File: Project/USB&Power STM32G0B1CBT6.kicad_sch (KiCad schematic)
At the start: 16 parts, among them J1 JST SH, J12 USB_C sink board 1.3mm, J2 Pico EZmate, Q1 AP40P05, U58 PRTR5V0U2X, U64 AP2112K-3.3

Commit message: backups
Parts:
- renumbered C53 to C59, C55 to C60, J12 to J2, R8 to R6, U64 to U54
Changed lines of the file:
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@@
 				)
 				(path "/7fa06d8b-464b-4050-a0fd-d319cc509390/482325c2-4a62-42d2-bd7f-adb26184afc4"
-					(reference "C62")
+					(reference "C61")
 					(unit 1)
 				)
@@
 				)
 				(path "/7fa06d8b-464b-4050-a0fd-d319cc509390/482325c2-4a62-42d2-bd7f-adb26184afc4"
-					(reference "#PWR0175")
+					(reference "#PWR0177")
 					(unit 1)
 				)
@@
 		(dnp no)
 		(fields_autoplaced yes)
-		(property "Reference" "U64"
+		(property "Reference" "U54"
 			(at 130.81 25.4 0)
 			(effects
@@
 			(project "vootington V4N STM32G0B1CBT6"
 				(path "/7fa06d8b-464b-4050-a0fd-d319cc509390/482325c2-4a62-42d2-bd7f-adb26184afc4"
-					(reference "U64")
+					(reference "U54")
 					(unit 1)
 				)
@@
 		(on_board yes)
 		(dnp no)
-		(property "Reference" "#PWR0169"
+		(property "Reference" "#PWR0174"
 			(at 153.035 71.12 0)
 			(effects
@@
 			(project "vootington V4N STM32G0B1CBT6"
 				(path "/7fa06d8b-464b-4050-a0fd-d319cc509390/482325c2-4a62-42d2-bd7f-adb26184afc4"
-					(reference "#PWR0169")
+					(reference "#PWR0174")
 					(unit 1)
 				)
@@
 		(on_board yes)
 		(dnp no)
-		(property "Reference" "#PWR0157"
+		(property "Reference" "#PWR0170"
 			(at 113.03 53.34 0)
 			(effects
@@
 			(project "vootington V4N STM32G0B1CBT6"
 				(path "/7fa06d8b-464b-4050-a0fd-d319cc509390/482325c2-4a62-42d2-bd7f-adb26184afc4"
-					(reference "#PWR0157")
+					(reference "#PWR0170")
 					(unit 1)
 				)
@@
 			(project "vootington V4N STM32G0B1CBT6"
 				(path "/7fa06d8b-464b-4050-a0fd-d319cc509390/482325c2-4a62-42d2-bd7f-adb26184afc4"
-					(reference "R2")
+					(reference "R7")
 					(unit 1)
 				)
@@
 		(on_board yes)
 		(dnp no)
-		(property "Reference" "R8"
+		(property "Reference" "R6"
 			(at 118.11 43.18 90)
 			(effects
@@
 			(project "vootington V4N STM32G0B1CBT6"
 				(path "/7fa06d8b-464b-4050-a0fd-d319cc509390/482325c2-4a62-42d2-bd7f-adb26184afc4"
-					(reference "R8")
+					(reference "R6")
 					(unit 1)
 				)
@@
 		(dnp no)
 		(fields_autoplaced yes)
-		(property "Reference" "#PWR0174"
+		(property "Reference" "#PWR0176"
 			(at 25.273 86.995 0)
 			(effects
@@
 			(project "vootington V4N STM32G0B1CBT6"
 				(path "/7fa06d8b-464b-4050-a0fd-d319cc509390/482325c2-4a62-42d2-bd7f-adb26184afc4"
-					(reference "#PWR0174")
+					(reference "#PWR0176")
 					(unit 1)
 				)
@@
 		(on_board yes)
 		(dnp no)
-		(property "Reference" "C55"
+		(property "Reference" "C60"
 			(at 101.854 42.672 0)
 			(effects
@@
 			(project "vootington V4N STM32G0B1CBT6"
 				(path "/7fa06d8b-464b-4050-a0fd-d319cc509390/482325c2-4a62-42d2-bd7f-adb26184afc4"
-					(reference "C55")
+					(reference "C60")
 					(unit 1)
 				)
@@
 			(project "vootington V4N STM32G0B1CBT6"
 				(path "/7fa06d8b-464b-4050-a0fd-d319cc509390/482325c2-4a62-42d2-bd7f-adb26184afc4"
-					(reference "J13")
+					(reference "J3")
 					(unit 1)
 				)
@@
 			(project "vootington V4N STM32G0B1CBT6"
 				(path "/7fa06d8b-464b-4050-a0fd-d319cc509390/482325c2-4a62-42d2-bd7f-adb26184afc4"
-					(reference "#PWR0178")
+					(reference "#PWR0180")
 					(unit 1)
 				)
@@
 			(project "vootington V4N STM32G0B1CBT6"
 				(path "/7fa06d8b-464b-4050-a0fd-d319cc509390/482325c2-4a62-42d2-bd7f-adb26184afc4"
-					(reference "#PWR0177")
+					(reference "#PWR0179")
 					(unit 1)
 				)
@@
 		(dnp no)
 		(fields_autoplaced yes)
-		(property "Reference" "#PWR0168"
+		(property "Reference" "#PWR0173"
 			(at 140.335 68.58 0)
 			(effects
@@
 			(project "vootington V4N STM32G0B1CBT6"
 				(path "/7fa06d8b-464b-4050-a0fd-d319cc509390/482325c2-4a62-42d2-bd7f-adb26184afc4"
-					(reference "#PWR0168")
+					(reference "#PWR0173")
 					(unit 1)
 				)
@@
 			(project "vootington V4N STM32G0B1CBT6"
 				(path "/7fa06d8b-464b-4050-a0fd-d319cc509390/482325c2-4a62-42d2-bd7f-adb26184afc4"
-					(reference "#PWR0180")
+					(reference "#PWR0182")
 					(unit 1)
 				)
@@
 			(project "vootington V4N STM32G0B1CBT6"
 				(path "/7fa06d8b-464b-4050-a0fd-d319cc509390/482325c2-4a62-42d2-bd7f-adb26184afc4"
-					(reference "#PWR0176")
+					(reference "#PWR0178")
 					(unit 1)
 				)
@@
 				)
 				(path "/7fa06d8b-464b-4050-a0fd-d319cc509390/482325c2-4a62-42d2-bd7f-adb26184afc4"
-					(reference "#PWR0170")
+					(reference "#PWR0169")
 					(unit 1)
 				)
@@
 				)
 				(path "/7fa06d8b-464b-4050-a0fd-d319cc509390/482325c2-4a62-42d2-bd7f-adb26184afc4"
-					(reference "#PWR0173")
+					(reference "#PWR0175")
 					(unit 1)
 				)
@@
 			(project "vootington V4N STM32G0B1CBT6"
 				(path "/7fa06d8b-464b-4050-a0fd-d319cc509390/482325c2-4a62-42d2-bd7f-adb26184afc4"
-					(reference "#PWR0179")
+					(reference "#PWR0181")
 					(unit 1)
 				)
@@
 				)
 				(path "/7fa06d8b-464b-4050-a0fd-d319cc509390/482325c2-4a62-42d2-bd7f-adb26184afc4"
-					(reference "C60")
+					(reference "C57")
 					(unit 1)
 				)
@@
 			(project "vootington V4N STM32G0B1CBT6"
 				(path "/7fa06d8b-464b-4050-a0fd-d319cc509390/482325c2-4a62-42d2-bd7f-adb26184afc4"
-					(reference "J14")
+					(reference "J4")
 					(unit 1)
 				)
@@
 			(project "vootington V4N STM32G0B1CBT6"
 				(path "/7fa06d8b-464b-4050-a0fd-d319cc509390/482325c2-4a62-42d2-bd7f-adb26184afc4"
-					(reference "#PWR0181")
+					(reference "#PWR0183")
 					(unit 1)
 				)
@@
 		(on_board yes)
 		(dnp no)
-		(property "Reference" "C53"
+		(property "Reference" "C59"
 			(at 148.336 35.306 0)
 			(effects
@@
 			(project "vootington V4N STM32G0B1CBT6"
 				(path "/7fa06d8b-464b-4050-a0fd-d319cc509390/482325c2-4a62-42d2-bd7f-adb26184afc4"
-					(reference "C53")
+					(reference "C59")
 					(unit 1)
 				)
@@
 		(dnp no)
 		(fields_autoplaced yes)
-		(property "Reference" "#PWR0165"
+		(property "Reference" "#PWR0168"
 			(at 140.97 34.29 0)
 			(effects
@@
 			(project "vootington V4N STM32G0B1CBT6"
 				(path "/7fa06d8b-464b-4050-a0fd-d319cc509390/482325c2-4a62-42d2-bd7f-adb26184afc4"
-					(reference "#PWR0165")
+					(reference "#PWR0168")
 					(unit 1)
 				)
@@
 			(project "vootington V4N STM32G0B1CBT6"
 				(path "/7fa06d8b-464b-4050-a0fd-d319cc509390/482325c2-4a62-42d2-bd7f-adb26184afc4"
-					(reference "R3")
+					(reference "R8")
 					(unit 1)
 				)
@@
 				)
 				(path "/7fa06d8b-464b-4050-a0fd-d319cc509390/482325c2-4a62-42d2-bd7f-adb26184afc4"
-					(reference "C61")
+					(reference "C58")
 					(unit 1)
 				)
@@
 		(dnp no)
 		(fields_autoplaced yes)
-		(property "Reference" "J12"
+		(property "Reference" "J2"
 			(at 29.21 33.02 0)
 			(effects
@@
 			(project "vootington V4N STM32G0B1CBT6"
 				(path "/7fa06d8b-464b-4050-a0fd-d319cc509390/482325c2-4a62-42d2-bd7f-adb26184afc4"
-					(reference "J12")
-					(unit 1)
-				)
+					(reference "J2")
+					(unit 1)
+				)

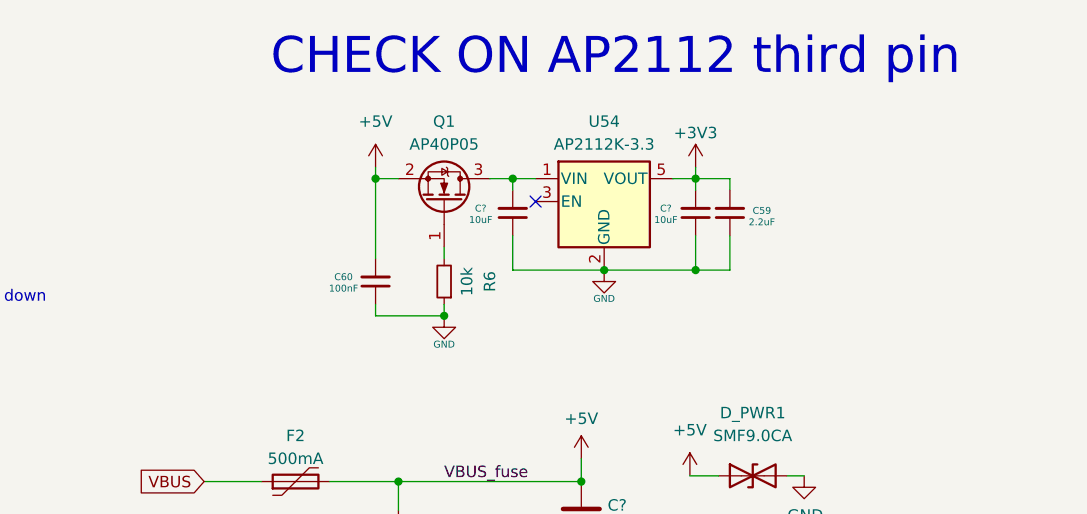
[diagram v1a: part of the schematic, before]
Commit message: power error fix
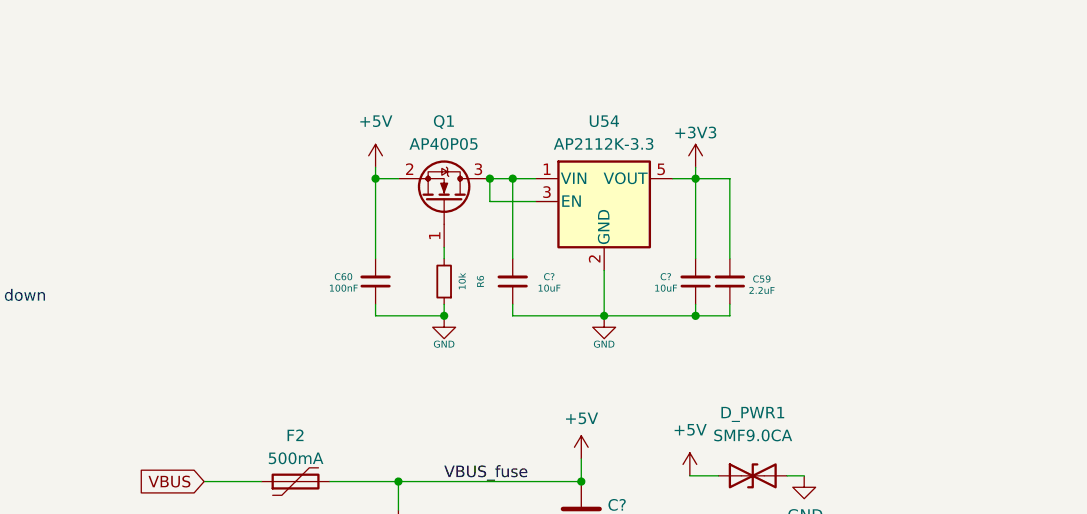
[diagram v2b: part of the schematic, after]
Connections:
- net at C?.2, Q1.3 (D), U54.1 (VIN): now also U54.3 (EN)
- no-connect marks 3 -> 2
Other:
- note removed: "CHECK ON AP2112 third pin"
- moved on the sheet: C59, C?
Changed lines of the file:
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@@
 	)
 	(junction
+		(at 118.11 31.75)
+		(diameter 0)
+		(color 0 0 0 0)
+	)
+	(junction
+		(at 130.81 46.99)
+		(diameter 0)
+		(color 0 0 0 0)
+	)
+	(junction
 		(at 140.97 31.75)
 		(diameter 0)
@@
 	)
 	(junction
-		(at 140.97 41.91)
+		(at 140.97 46.99)
 		(diameter 0)
 		(color 0 0 0 0)
@@
 		(color 0 0 0 0)
 	)
-	(junction
-		(at 130.81 41.91)
-		(diameter 0)
-		(color 0 0 0 0)
-	)
 	(no_connect
 		(at 44.45 68.58)
@@
 		(at 44.45 71.12)
 	)
-	(no_connect
-		(at 123.19 34.29)
-	)
 	(wire
 		(pts
@@
 		)
 	)
-	(bus
-		(pts
-			(xy 13.97 104.775) (xy 49.657 104.775)
-		)
-		(stroke
-			(width 0)
-			(type default)
-		)
-	)
 	(wire
 		(pts
-			(xy 140.97 31.75) (xy 140.97 33.02)
+			(xy 144.78 46.99) (xy 144.78 45.72)
 		)
 		(stroke
@@
 		)
 	)
-	(wire
+	(bus
 		(pts
-			(xy 45.72 54.61) (xy 46.99 54.61)
+			(xy 13.97 104.775) (xy 49.657 104.775)
 		)
 		(stroke
@@
 	(wire
 		(pts
-			(xy 140.97 38.1) (xy 140.97 41.91)
+			(xy 140.97 31.75) (xy 140.97 40.64)
 		)
 		(stroke
@@
 	(wire
 		(pts
-			(xy 120.65 38.1) (xy 120.65 41.91)
+			(xy 45.72 54.61) (xy 46.99 54.61)
 		)
 		(stroke
 			(width 0)
-			(type solid)
+			(type default)
 		)
 	)
@@
 	(wire
 		(pts
+			(xy 118.11 31.75) (xy 118.11 34.29)
+		)
+		(stroke
+			(width 0)
+			(type default)
+		)
+	)
+	(wire
+		(pts
 			(xy 151.13 64.77) (xy 153.035 64.77)
 		)
@@
 	(wire
 		(pts
-			(xy 144.78 31.75) (xy 144.78 33.02)
+			(xy 144.78 31.75) (xy 144.78 40.64)
+		)
+		(stroke
+			(width 0)
+			(type default)
+		)
+	)
+	(wire
+		(pts
+			(xy 118.11 34.29) (xy 123.19 34.29)
 		)
 		(stroke
@@
 	(wire
 		(pts
-			(xy 130.81 41.91) (xy 140.97 41.91)
+			(xy 120.65 46.99) (xy 120.65 45.72)
+		)
+		(stroke
+			(width 0)
+			(type solid)
+		)
+	)
+	(wire
+		(pts
+			(xy 130.81 46.99) (xy 140.97 46.99)
 		)
 		(stroke
@@
 	(wire
 		(pts
-			(xy 105.41 45.72) (xy 105.41 46.99)
+			(xy 130.81 41.91) (xy 130.81 46.99)
 		)
 		(stroke
 			(width 0)
-			(type default)
+			(type solid)
 		)
 	)
 	(wire
 		(pts
-			(xy 105.41 31.75) (xy 105.41 40.64)
+			(xy 105.41 45.72) (xy 105.41 46.99)
 		)
 		(stroke
@@
 		)
 	)
-	(bus
+	(wire
 		(pts
-			(xy 86.995 104.775) (xy 86.995 131.953)
+			(xy 105.41 31.75) (xy 105.41 40.64)
 		)
 		(stroke
@@
 		)
 	)
-	(wire
+	(bus
 		(pts
-			(xy 144.78 38.1) (xy 144.78 41.91)
+			(xy 86.995 104.775) (xy 86.995 131.953)
 		)
 		(stroke
@@
 	(wire
 		(pts
-			(xy 140.97 41.91) (xy 144.78 41.91)
+			(xy 140.97 46.99) (xy 144.78 46.99)
 		)
 		(stroke
@@
 	(wire
 		(pts
+			(xy 140.97 46.99) (xy 140.97 45.72)
+		)
+		(stroke
+			(width 0)
+			(type solid)
+		)
+	)
+	(wire
+		(pts
 			(xy 55.245 46.99) (xy 55.245 45.72)
 		)
@@
 	(wire
 		(pts
-			(xy 120.65 31.75) (xy 120.65 33.02)
+			(xy 120.65 31.75) (xy 120.65 40.64)
 		)
 		(stroke
@@
 	(wire
 		(pts
-			(xy 120.65 41.91) (xy 130.81 41.91)
+			(xy 120.65 46.99) (xy 130.81 46.99)
 		)
 		(stroke
@@
 		)
 	)
-	(text "CHECK ON AP2112 third pin"
-		(exclude_from_sim no)
-		(at 132.08 18.288 0)
-		(effects
-			(font
-				(size 4 4)
-			)
-		)
-	)
 	(text "Pico EZmate"
 		(exclude_from_sim no)
@@
 	(label "VBUS_fuse"
 		(at 113.03 65.405 0)
-		(fields_autoplaced yes)
 		(effects
 			(font
@@
 		(dnp no)
 		(property "Reference" "R6"
-			(at 118.11 43.18 90)
+			(at 117.094 43.18 90)
 			(effects
 				(font
-					(size 1.27 1.27)
+					(size 0.762 0.762)
 				)
 			)
 		)
 		(property "Value" "10k"
-			(at 115.57 43.18 90)
+			(at 115.062 43.18 90)
 			(effects
 				(font
-					(size 1.27 1.27)
+					(size 0.762 0.762)
 				)
 			)
@@
 	(symbol
 		(lib_id "power:GND")
-		(at 130.81 41.91 0)
+		(at 130.81 46.99 0)
 		(unit 1)
 		(exclude_from_sim no)
@@
 		(dnp no)
 		(property "Reference" "#PWR?"
-			(at 130.81 48.26 0)
+			(at 130.81 53.34 0)
 			(effects
 				(font
@@
 		)
 		(property "Value" "GND"
-			(at 130.81 45.085 0)
+			(at 130.81 50.165 0)
 			(effects
 				(font
@@
 		)
 		(property "Footprint" ""
-			(at 130.81 41.91 0)
+			(at 130.81 46.99 0)
 			(effects
 				(font
@@
 		)
 		(property "Datasheet" ""
-			(at 130.81 41.91 0)
+			(at 130.81 46.99 0)
 			(effects
 				(font
@@
 		)
 		(property "Description" ""
-			(at 130.81 41.91 0)
+			(at 130.81 46.99 0)
 			(effects
 				(font
@@
 	(symbol
 		(lib_id "Device:C_Small")
-		(at 120.65 35.56 180)
+		(at 120.65 43.18 180)
 		(unit 1)
 		(exclude_from_sim no)
@@
 		(dnp no)
 		(property "Reference" "C?"
-			(at 117.094 35.052 0)
+			(at 124.714 42.672 0)
 			(effects
 				(font
@@
 		)
 		(property "Value" "10uF"
-			(at 117.094 36.322 0)
+			(at 124.714 43.942 0)
 			(effects
 				(font
@@
 		)
 		(property "Footprint" "Capacitor_SMD:C_0402_1005Metric"
-			(at 120.65 35.56 0)
+			(at 120.65 43.18 0)
 			(effects
 				(font
@@
 		)
 		(property "Datasheet" "~"
-			(at 120.65 35.56 0)
+			(at 120.65 43.18 0)
 			(effects
 				(font
@@
 		)
 		(property "Description" ""
-			(at 120.65 35.56 0)
+			(at 120.65 43.18 0)
 			(effects
 				(font
@@
 		)
 		(property "LCSC" "C52923"
-			(at 120.65 35.56 0)
+			(at 120.65 43.18 0)
 			(effects
 				(font
@@
 	(symbol
 		(lib_id "Device:C_Small")
-		(at 144.78 35.56 180)
+		(at 144.78 43.18 180)
 		(unit 1)
 		(exclude_from_sim no)
@@
 		(dnp no)
 		(property "Reference" "C59"
-			(at 148.336 35.306 0)
+			(at 148.336 42.926 0)
 			(effects
 				(font
@@
 		)
 		(property "Value" "2.2uF"
-			(at 148.336 36.576 0)
+			(at 148.336 44.196 0)
 			(effects
 				(font
@@
 		)
 		(property "Footprint" "Capacitor_SMD:C_0402_1005Metric"
-			(at 144.78 35.56 0)
+			(at 144.78 43.18 0)
 			(effects
 				(font
@@
 		)
 		(property "Datasheet" "~"
-			(at 144.78 35.56 0)
+			(at 144.78 43.18 0)
 			(effects
 				(font
@@
 		)
 		(property "Description" ""
-			(at 144.78 35.56 0)
+			(at 144.78 43.18 0)
 			(effects
 				(font
@@
 		)
 		(property "LCSC" "C52923"
-			(at 144.78 35.56 0)
+			(at 144.78 43.18 0)
 			(effects
 				(font
@@
 	(symbol
 		(lib_id "Device:C_Small")
-		(at 140.97 35.56 180)
+		(at 140.97 43.18 180)
 		(unit 1)
 		(exclude_from_sim no)
@@
 		(dnp no)
 		(property "Reference" "C?"
-			(at 137.668 35.052 0)
+			(at 137.668 42.672 0)
 			(effects
 				(font
@@
 		)
 		(property "Value" "10uF"
-			(at 137.668 36.322 0)
+			(at 137.668 43.942 0)
 			(effects
 				(font
@@
 		)
 		(property "Footprint" "Capacitor_SMD:C_0402_1005Metric"
-			(at 140.97 35.56 0)
+			(at 140.97 43.18 0)
 			(effects
 				(font
@@
 		)
 		(property "Datasheet" "~"
-			(at 140.97 35.56 0)
+			(at 140.97 43.18 0)
 			(effects
 				(font
@@
 		)
 		(property "Description" ""
-			(at 140.97 35.56 0)
+			(at 140.97 43.18 0)
 			(effects
 				(font
@@
 		)
 		(property "LCSC" "C52923"
-			(at 140.97 35.56 0)
+			(at 140.97 43.18 0)
 			(effects
 				(font
